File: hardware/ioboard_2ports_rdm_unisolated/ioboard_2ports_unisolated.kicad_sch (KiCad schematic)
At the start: 29 parts

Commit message: Finish IO-Board updates
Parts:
- C1, C4: value (none) -> 22uF; footprint (none) -> Capacitor_SMD:C_0805_2012Metric
- C2, C3: value (none) -> 100nF; footprint (none) -> Capacitor_SMD:C_0603_1608Metric
- DO_NOT_MOUNT_J4: value (none) -> Conn_01x01_DO_NOT_MOUNT; footprint (none) -> Connector_PinHeader_1.00mm:PinHeader_1x02_P1.00mm_Vertical_SMD_Pin1Left
- H1, H2, H3, H4: value (none) -> MountingHole; footprint (none) -> MountingHole:MountingHole_3.2mm_M3
- J1: value (none) -> Conn_02x06_Odd_Even; footprint (none) -> Connector_PinHeader_2.54mm:PinHeader_2x06_P2.54mm_Vertical
- J12, J6: value (none) -> Conn_01x03; footprint (none) -> Connector_PinHeader_2.54mm:PinHeader_1x03_P2.54mm_Vertical
- J2, J8: value (none) -> XLR3; footprint (none) -> Connector_Audio:Jack_XLR_Neutrik_NC3FAAH_Horizontal
- J3, J9: value (none) -> XLR3; footprint (none) -> NC3FD-H:Jack_XLR_Neutrik_NC3FD-H_Horizontal
- R1, R11, R17, R7: value (none) -> 680R; footprint (none) -> Resistor_SMD:R_0603_1608Metric_Pad0.98x0.95mm_HandSolder
- R15, R5: value (none) -> 120R; footprint (none) -> Resistor_SMD:R_0603_1608Metric_Pad0.98x0.95mm_HandSolder
- R2, R3: value (none) -> 2k; footprint (none) -> Resistor_SMD:R_0603_1608Metric
- R4: value (none) -> 1R; footprint (none) -> Resistor_SMD:R_0805_2012Metric
- U1: value (none) -> M24C64-RMN6TP; footprint (none) -> Package_SO:SOIC-8_3.9x4.9mm_P1.27mm; LCSC C7562 -> C79988
- U2, U4: value (none) -> SP3485EN; footprint (none) -> Package_SO:SOIC-8_3.9x4.9mm_P1.27mm
- U3: value (none) -> AMS1117-3.3; footprint (none) -> Package_TO_SOT_SMD:SOT-223
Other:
- note added: "I2C EEPROM for board identification and configuration storage"
- note removed: "I2C EEPROM for board identification"
- title: rp2040_dongle_ioboard_2ports_rdm_unisolated -> rp2040_dongle_ioboard_2ports_unisolated

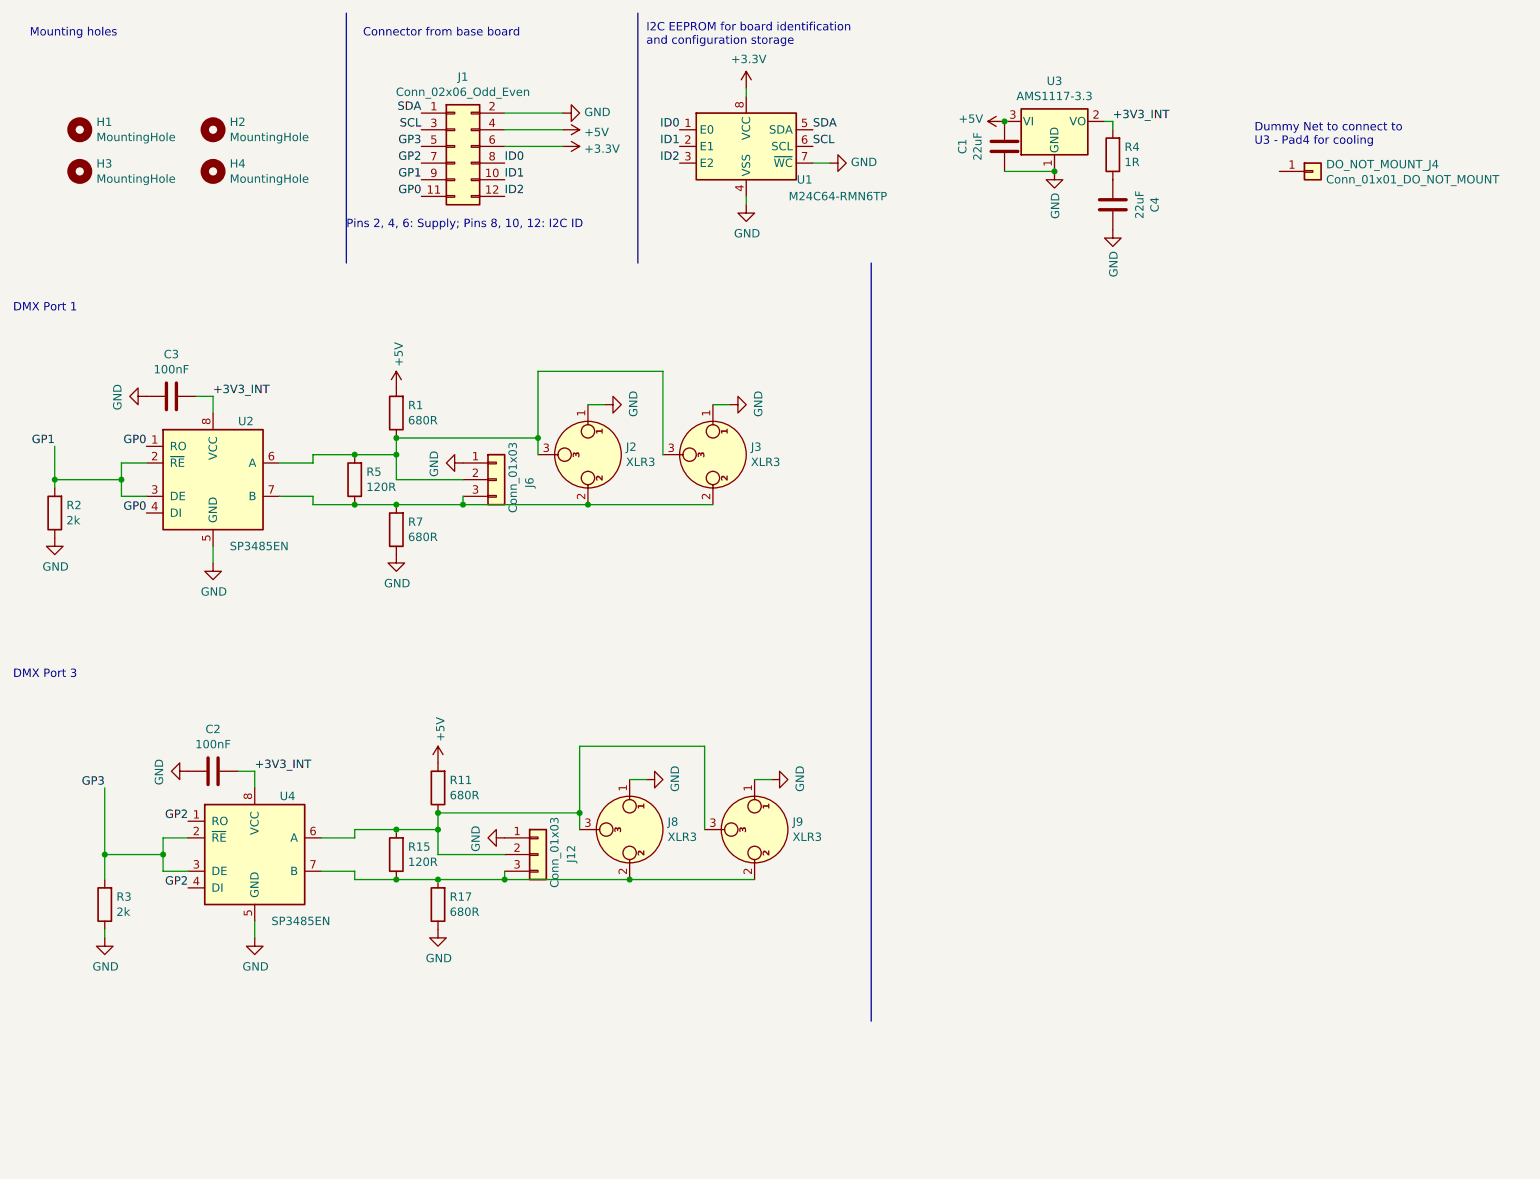
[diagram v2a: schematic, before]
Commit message: Add RJ45 jacks to ioboard_2ports_rdm_unisolated as well
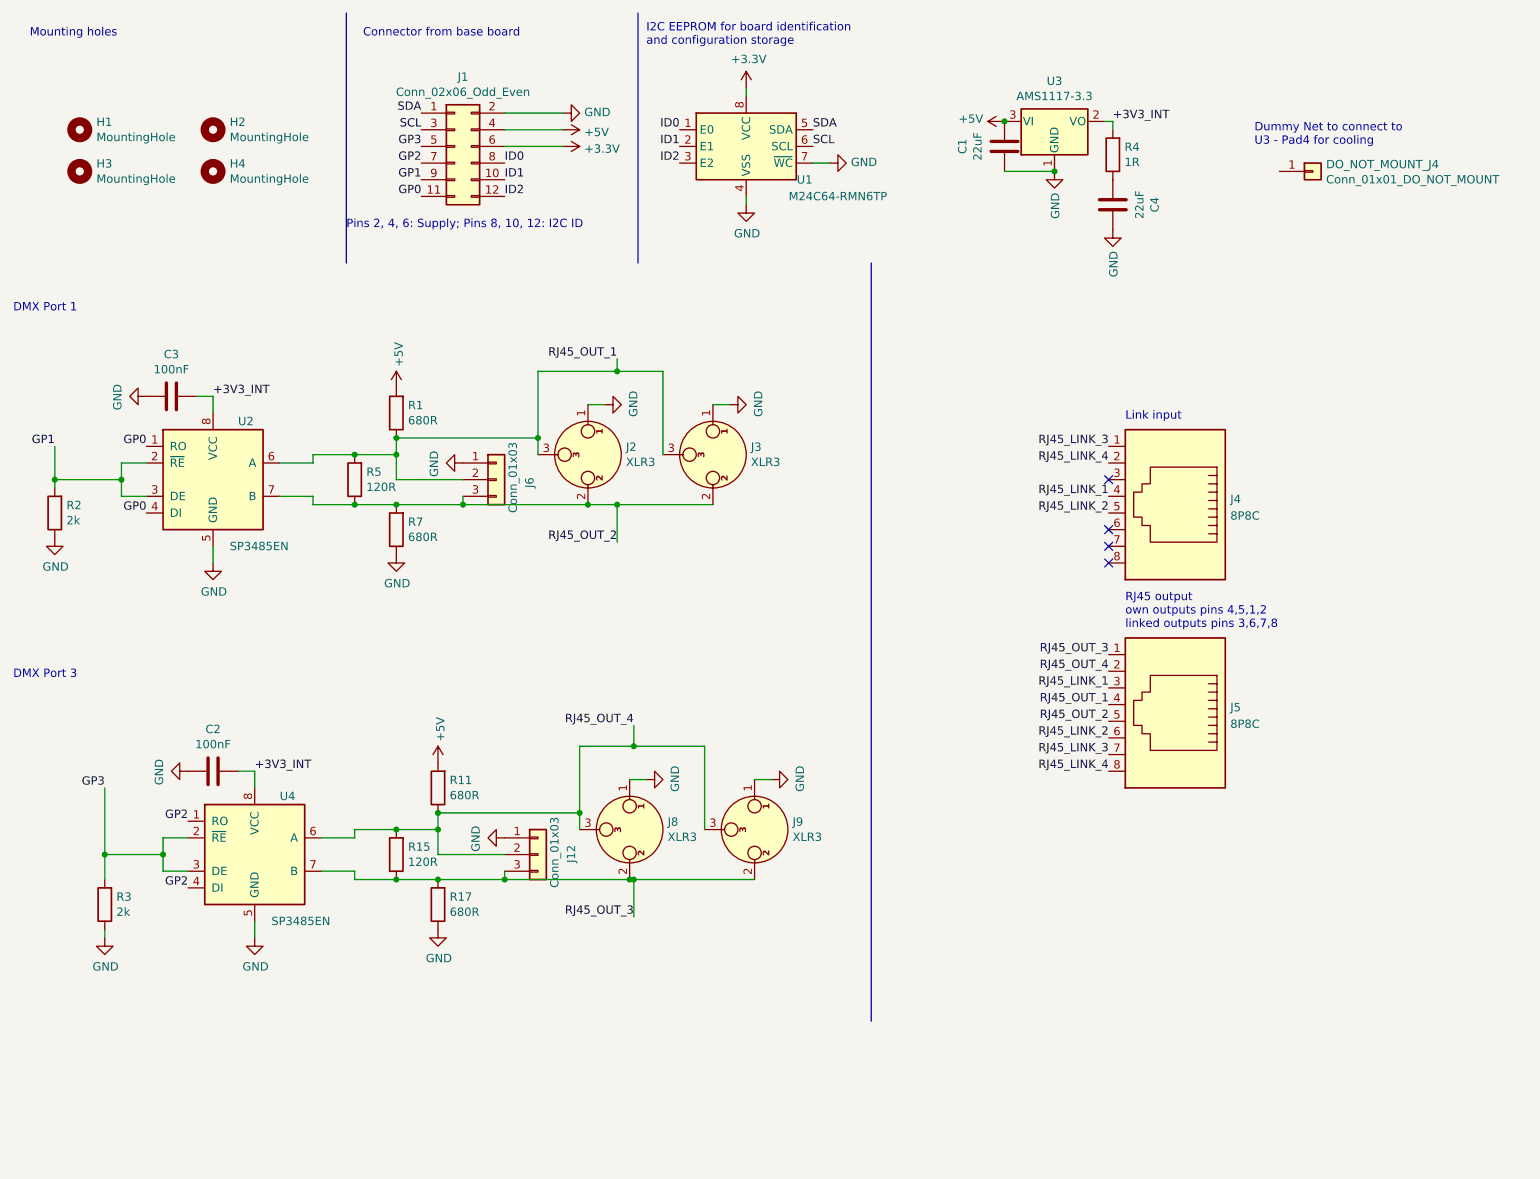
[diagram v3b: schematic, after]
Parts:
- added J4, J5: 8P8C, RJ45_Sparkfun:RJ45_Sparkfun, symbol Connector:8P8C
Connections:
- net RJ45_OUT_1: now reaches J2.3, J3.3, J6.2 (Pin_2), R1.1, R5.2, U2.6 (A)
- net RJ45_OUT_1: now also J5.4
- net RJ45_OUT_2: now reaches J2.2, J3.2, J6.3 (Pin_3), R5.1, R7.2, U2.7 (B)
- net RJ45_OUT_2: now also J5.5
- net RJ45_OUT_3: now reaches J12.3 (Pin_3), J8.2, J9.2, R15.1, R17.2, U4.7 (B)
- net RJ45_OUT_3: now also J5.1
- net RJ45_OUT_4: now reaches J12.2 (Pin_2), J8.3, J9.3, R11.1, R15.2, U4.6 (A)
- net RJ45_OUT_4: now also J5.2
- new net RJ45_LINK_1: J4.4, J5.3
- new net RJ45_LINK_2: J4.5, J5.6
- new net RJ45_LINK_3: J4.1, J5.7
- new net RJ45_LINK_4: J4.2, J5.8
- no-connect marks 0 -> 4
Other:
- note added: "Link input"
- note added: "RJ45 output own outputs pins 4,5,1,2 linked outputs pins 3,6,7,8"
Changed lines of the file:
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@@
     (title "rp2040_dongle_ioboard_2ports_unisolated")
     (date "2022-11-09")
-    (rev "0.5")
+    (rev "0.6")
     (company "https://www.openlighting.org")
   )
+  (junction (at 107.315 144.78) (diameter 0) (color 0 0 0 0)
+  )
   (junction (at 35.56 140.97) (diameter 0) (color 0 0 0 0)
   )
@@
   (junction (at 71.12 144.78) (diameter 0) (color 0 0 0 0)
   )
+  (junction (at 107.315 124.46) (diameter 0) (color 0 0 0 0)
+  )
   (junction (at 87.63 144.78) (diameter 0) (color 0 0 0 0)
   )
@@
   (junction (at 71.12 77.47) (diameter 0) (color 0 0 0 0)
   )
+  (junction (at 104.775 87.63) (diameter 0) (color 0 0 0 0)
+  )
   (junction (at 81.28 87.63) (diameter 0) (color 0 0 0 0)
   )
   (junction (at 77.47 144.78) (diameter 0) (color 0 0 0 0)
   )
+  (junction (at 104.775 67.31) (diameter 0) (color 0 0 0 0)
+  )
+  (no_connect (at 179.705 93.98))
+  (no_connect (at 179.705 91.44))
+  (no_connect (at 179.705 83.82))
+  (no_connect (at 179.705 96.52))
   (wire (pts (xy 58.42 87.63) (xy 64.77 87.63))
     (stroke (width 0) (type default) (color 0 0 0 0))
@@
     (stroke (width 0) (type default) (color 0 0 0 0))
   )
+  (wire (pts (xy 107.315 124.46) (xy 118.11 124.46))
+    (stroke (width 0) (type default) (color 0 0 0 0))
+  )
+  (wire (pts (xy 104.775 87.63) (xy 119.38 87.63))
+    (stroke (width 0) (type default) (color 0 0 0 0))
+  )
   (wire (pts (xy 64.77 144.78) (xy 71.12 144.78))
     (stroke (width 0) (type default) (color 0 0 0 0))
@@
     (stroke (width 0) (type default) (color 0 0 0 0))
   )
+  (wire (pts (xy 104.775 67.31) (xy 111.76 67.31))
+    (stroke (width 0) (type default) (color 0 0 0 0))
+  )
   (wire (pts (xy 71.12 83.82) (xy 81.28 83.82))
     (stroke (width 0) (type default) (color 0 0 0 0))
@@
     (stroke (width 0) (type default) (color 0 0 0 0))
   )
+  (wire (pts (xy 107.315 150.495) (xy 107.315 144.78))
+    (stroke (width 0) (type default) (color 0 0 0 0))
+  )
+  (wire (pts (xy 104.775 65.405) (xy 104.775 67.31))
+    (stroke (width 0) (type default) (color 0 0 0 0))
+  )
   (wire (pts (xy 71.12 80.01) (xy 71.12 83.82))
     (stroke (width 0) (type default) (color 0 0 0 0))
@@
     (stroke (width 0) (type default) (color 0 0 0 0))
   )
+  (wire (pts (xy 107.315 121.285) (xy 107.315 124.46))
+    (stroke (width 0) (type default) (color 0 0 0 0))
+  )
   (wire (pts (xy 171.45 36.83) (xy 163.83 36.83))
     (stroke (width 0) (type default) (color 0 0 0 0))
   )
+  (wire (pts (xy 104.775 87.63) (xy 104.775 93.345))
+    (stroke (width 0) (type default) (color 0 0 0 0))
+  )
   (wire (pts (xy 39.37 138.43) (xy 35.56 138.43))
     (stroke (width 0) (type default) (color 0 0 0 0))
@@
     (stroke (width 0) (type default) (color 0 0 0 0))
   )
-  (wire (pts (xy 100.33 87.63) (xy 119.38 87.63))
+  (wire (pts (xy 100.33 87.63) (xy 104.775 87.63))
     (stroke (width 0) (type default) (color 0 0 0 0))
   )
@@
     (stroke (width 0) (type default) (color 0 0 0 0))
   )
-  (wire (pts (xy 99.06 124.46) (xy 118.11 124.46))
-    (stroke (width 0) (type default) (color 0 0 0 0))
-  )
-  (wire (pts (xy 92.71 67.31) (xy 111.76 67.31))
+  (wire (pts (xy 99.06 124.46) (xy 107.315 124.46))
+    (stroke (width 0) (type default) (color 0 0 0 0))
+  )
+  (wire (pts (xy 92.71 67.31) (xy 104.775 67.31))
     (stroke (width 0) (type default) (color 0 0 0 0))
   )
@@
     (stroke (width 0) (type default) (color 0 0 0 0))
   )
+  (wire (pts (xy 107.315 144.78) (xy 125.73 144.78))
+    (stroke (width 0) (type default) (color 0 0 0 0))
+  )
   (wire (pts (xy 71.12 144.78) (xy 77.47 144.78))
     (stroke (width 0) (type default) (color 0 0 0 0))
   )
-  (wire (pts (xy 106.68 144.78) (xy 125.73 144.78))
+  (wire (pts (xy 106.68 144.78) (xy 107.315 144.78))
     (stroke (width 0) (type default) (color 0 0 0 0))
   )
@@
     (stroke (width 0) (type default) (color 0 0 0 0))
   )
+  (text "RJ45 output\nown outputs pins 4,5,1,2\nlinked outputs pins 3,6,7,8"
+    (at 182.245 106.68 0)
+    (effects (font (size 1.27 1.27)) (justify left bottom))
+  )
   (text "Dummy Net to connect to\nU3 - Pad4 for cooling" (at 201.93 33.02 0)
     (effects (font (size 1.27 1.27)) (justify left bottom))
@@
   )
   (text "DMX Port 3" (at 12.7 114.3 0)
+    (effects (font (size 1.27 1.27)) (justify left bottom))
+  )
+  (text "Link input" (at 182.245 74.93 0)
     (effects (font (size 1.27 1.27)) (justify left bottom))
   )
@@
     (effects (font (size 1.27 1.27)) (justify left bottom))
   )
+  (label "RJ45_LINK_4" (at 179.705 128.27 180)
+    (effects (font (size 1.27 1.27)) (justify right bottom))
+  )
+  (label "RJ45_OUT_1" (at 104.775 65.405 180)
+    (effects (font (size 1.27 1.27)) (justify right bottom))
+  )
+  (label "RJ45_OUT_3" (at 107.315 150.495 180)
+    (effects (font (size 1.27 1.27)) (justify right bottom))
+  )
+  (label "RJ45_LINK_3" (at 179.705 125.73 180)
+    (effects (font (size 1.27 1.27)) (justify right bottom))
+  )
   (label "ID2" (at 87.63 40.64 0)
     (effects (font (size 1.27 1.27)) (justify left bottom))
   )
+  (label "RJ45_LINK_2" (at 179.705 123.19 180)
+    (effects (font (size 1.27 1.27)) (justify right bottom))
+  )
   (label "GP2" (at 39.37 146.05 180)
     (effects (font (size 1.27 1.27)) (justify right bottom))
@@
     (effects (font (size 1.27 1.27)) (justify right bottom))
   )
+  (label "RJ45_OUT_4" (at 179.705 113.03 180)
+    (effects (font (size 1.27 1.27)) (justify right bottom))
+  )
   (label "ID2" (at 114.3 35.56 180)
     (effects (font (size 1.27 1.27)) (justify right bottom))
@@
     (effects (font (size 1.27 1.27)) (justify right bottom))
   )
+  (label "RJ45_LINK_1" (at 179.705 86.36 180)
+    (effects (font (size 1.27 1.27)) (justify right bottom))
+  )
   (label "+3V3_INT" (at 180.34 29.21 0)
     (effects (font (size 1.27 1.27)) (justify left bottom))
@@
     (effects (font (size 1.27 1.27)) (justify right bottom))
   )
+  (label "RJ45_OUT_2" (at 104.775 93.345 180)
+    (effects (font (size 1.27 1.27)) (justify right bottom))
+  )
   (label "SDA" (at 134.62 30.48 0)
     (effects (font (size 1.27 1.27)) (justify left bottom))
@@
     (effects (font (size 1.27 1.27)) (justify right bottom))
   )
+  (label "RJ45_LINK_3" (at 179.705 78.74 180)
+    (effects (font (size 1.27 1.27)) (justify right bottom))
+  )
   (label "GP0" (at 74.93 40.64 180)
     (effects (font (size 1.27 1.27)) (justify right bottom))
   )
+  (label "RJ45_OUT_4" (at 107.315 121.285 180)
+    (effects (font (size 1.27 1.27)) (justify right bottom))
+  )
+  (label "RJ45_LINK_4" (at 179.705 81.28 180)
+    (effects (font (size 1.27 1.27)) (justify right bottom))
+  )
+  (label "RJ45_OUT_2" (at 179.705 120.65 180)
+    (effects (font (size 1.27 1.27)) (justify right bottom))
+  )
   (label "ID1" (at 87.63 38.1 0)
     (effects (font (size 1.27 1.27)) (justify left bottom))
@@
   (label "+3V3_INT" (at 43.18 71.12 0)
     (effects (font (size 1.27 1.27)) (justify left bottom))
+  )
+  (label "RJ45_OUT_3" (at 179.705 110.49 180)
+    (effects (font (size 1.27 1.27)) (justify right bottom))
+  )
+  (label "RJ45_OUT_1" (at 179.705 118.11 180)
+    (effects (font (size 1.27 1.27)) (justify right bottom))
+  )
+  (label "RJ45_LINK_1" (at 179.705 115.57 180)
+    (effects (font (size 1.27 1.27)) (justify right bottom))
+  )
+  (label "RJ45_LINK_2" (at 179.705 88.9 180)
+    (effects (font (size 1.27 1.27)) (justify right bottom))
   )
   (symbol (lib_id "Connector_Generic:Conn_02x06_Odd_Even") (at 80.01 33.02 0) (unit 1)
@@
     (pin "3")
   )
+  (symbol (lib_id "Connector:8P8C") (at 189.865 118.11 180) (unit 1)
+    (in_bom yes) (on_board yes) (fields_autoplaced)
+    (property "Reference" "J5" (id 0) (at 198.247 118.5453 0)
+      (effects (font (size 1.27 1.27)) (justify right))
+    )
+    (property "Value" "8P8C" (id 1) (at 198.247 121.0822 0)
+      (effects (font (size 1.27 1.27)) (justify right))
+    )
+    (property "Footprint" "RJ45_Sparkfun:RJ45_Sparkfun" (id 2) (at 189.865 118.745 90)
+      (effects (font (size 1.27 1.27)) hide)
+    )
+    (property "Datasheet" "~" (id 3) (at 189.865 118.745 90)
+      (effects (font (size 1.27 1.27)) hide)
+    )
+    (pin "1")
+    (pin "2")
+    (pin "3")
+    (pin "4")
+    (pin "5")
+    (pin "6")
+    (pin "7")
+    (pin "8")
+  )
+  (symbol (lib_id "Connector:8P8C") (at 189.865 86.36 180) (unit 1)
+    (in_bom yes) (on_board yes) (fields_autoplaced)
+    (property "Reference" "J4" (id 0) (at 198.247 86.7953 0)
+      (effects (font (size 1.27 1.27)) (justify right))
+    )
+    (property "Value" "8P8C" (id 1) (at 198.247 89.3322 0)
+      (effects (font (size 1.27 1.27)) (justify right))
+    )
+    (property "Footprint" "RJ45_Sparkfun:RJ45_Sparkfun" (id 2) (at 189.865 86.995 90)
+      (effects (font (size 1.27 1.27)) hide)
+    )
+    (property "Datasheet" "~" (id 3) (at 189.865 86.995 90)
+      (effects (font (size 1.27 1.27)) hide)
+    )
+    (pin "1")
+    (pin "2")
+    (pin "3")
+    (pin "4")
+    (pin "5")
+    (pin "6")
+    (pin "7")
+    (pin "8")
+  )
   (sheet_instances
     (path "/" (page "1"))
@@
       (reference "J3") (unit 1) (value "XLR3") (footprint "NC3FD-H:Jack_XLR_Neutrik_NC3FD-H_Horizontal")
     )
+    (path "/dda1712d-97d0-4f96-9863-4da1d21c8917"
+      (reference "J4") (unit 1) (value "8P8C") (footprint "RJ45_Sparkfun:RJ45_Sparkfun")
+    )
+    (path "/74ca71f6-88da-4048-ab63-475af07a28c6"
+      (reference "J5") (unit 1) (value "8P8C") (footprint "RJ45_Sparkfun:RJ45_Sparkfun")
+    )
     (path "/00000000-0000-0000-0000-00006059f495"
